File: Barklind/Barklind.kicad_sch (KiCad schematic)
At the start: 7 parts, among them J1 Molex 47053-1000, J2 Molex 47053-1000, J3 Molex 47053-1000, J4 RJ45_Abracon_ARJP11A-MASA-B-A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, J5 Conn_01x19, J6 Conn_01x19, U4 ESP32-DevKitC

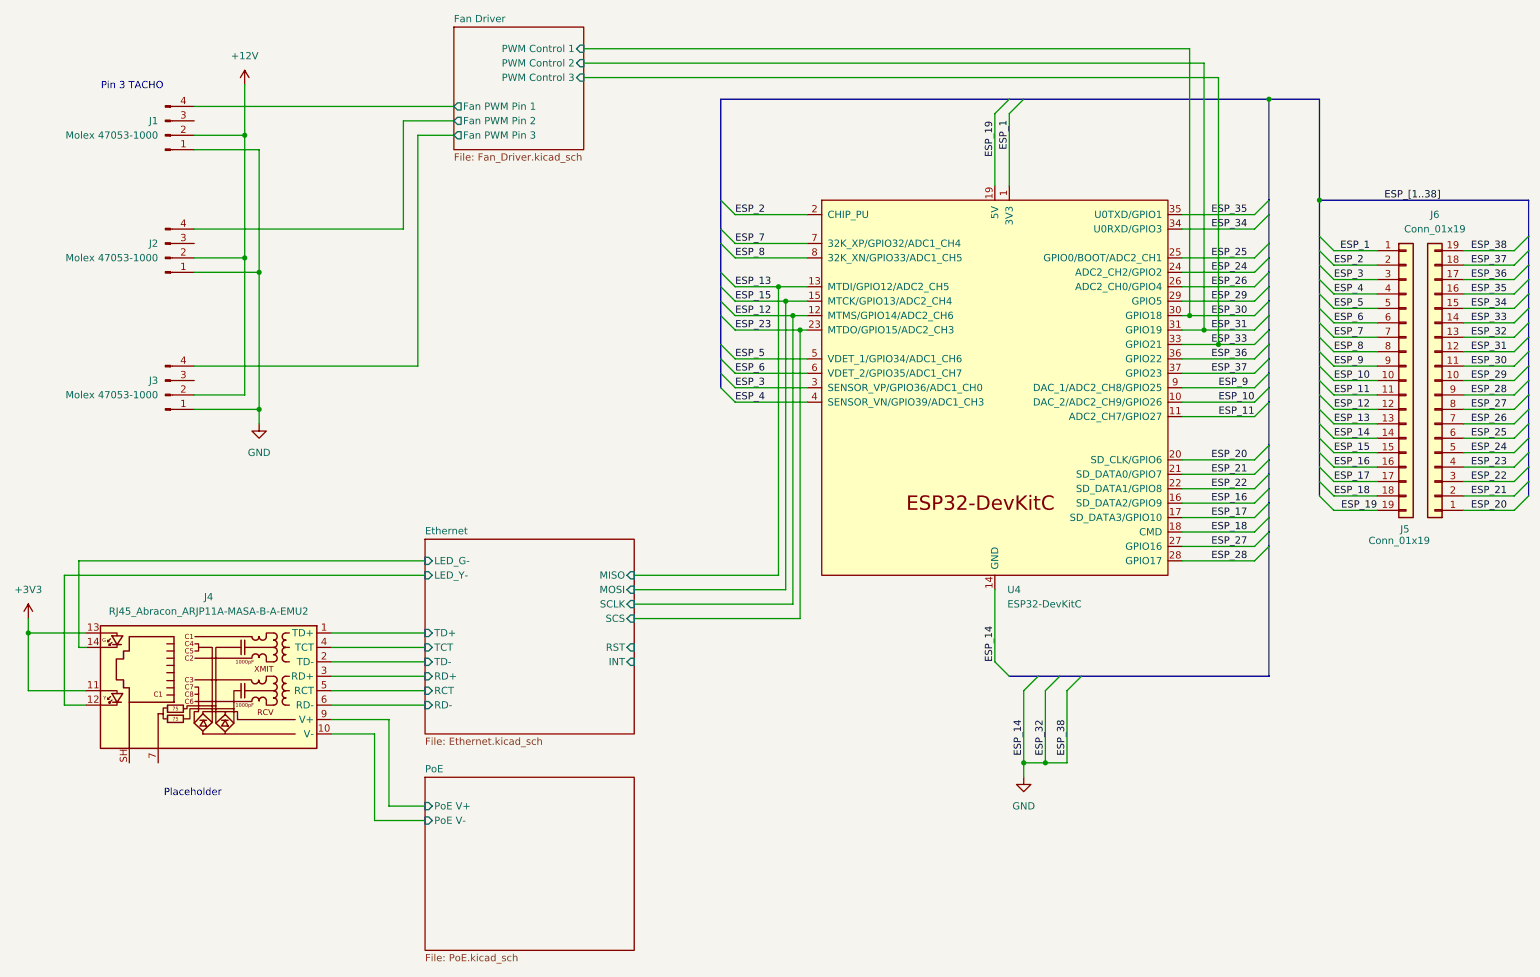
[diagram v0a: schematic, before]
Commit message: Added basic board (with no layout specified) Added additional comments to schematic
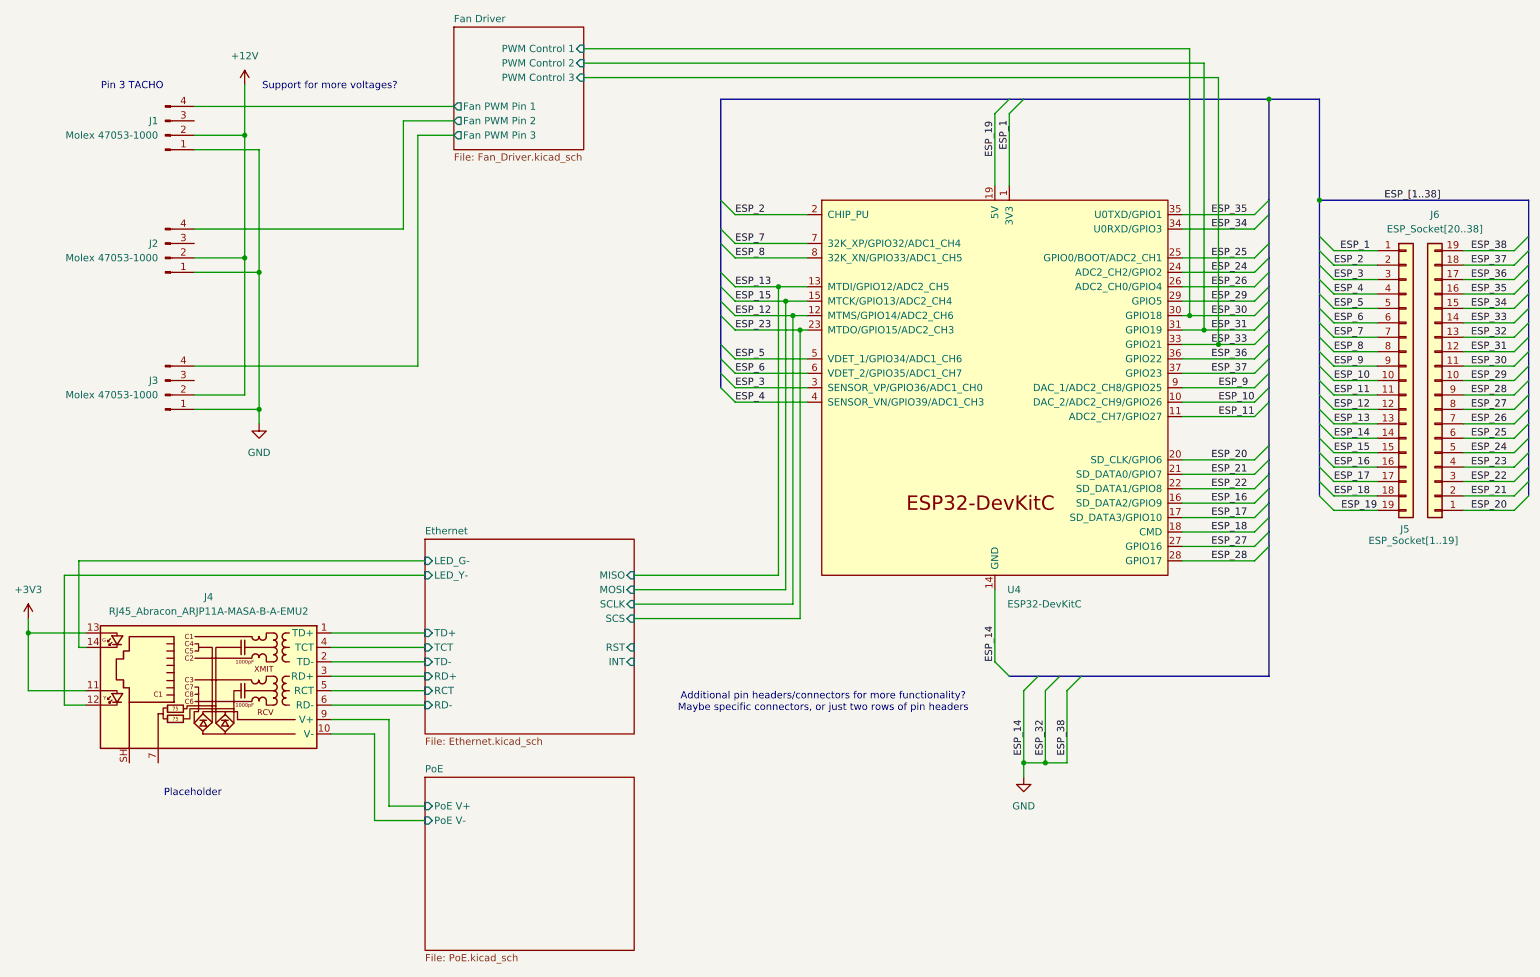
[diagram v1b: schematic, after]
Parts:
- J1, J2, J3: footprint (none) -> Connector:FanPinHeader_1x04_P2.54mm_Vertical
- J5: value Conn_01x19 -> ESP_Socket[1..19]; footprint (none) -> Connector_PinSocket_2.54mm:PinSocket_1x19_P2.54mm_Vertical
- J6: value Conn_01x19 -> ESP_Socket[20..38]; footprint (none) -> Connector_PinSocket_2.54mm:PinSocket_1x19_P2.54mm_Vertical
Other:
- note added: "Additional pin headers/connectors for more functionality? Maybe specific connectors, or just two rows of pin headers"
- note added: "Support for more voltages?"
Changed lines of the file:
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@@
+		)
+	)
+	(text "Support for more voltages?"
+		(exclude_from_sim no)
+		(at 68.326 38.354 0)
+		(effects
+			(font
+				(size 1.27 1.27)
+			)
 		)
 	)
@@
 		(exclude_from_sim no)
 		(at 44.196 162.814 0)
+		(effects
+			(font
+				(size 1.27 1.27)
+			)
+		)
+	)
+	(text "Additional pin headers/connectors for more functionality?\nMaybe specific connectors, or just two rows of pin headers\n"
+		(exclude_from_sim no)
+		(at 155.194 146.812 0)
 		(effects
 			(font
@@
 			)
 		)
-		(property "Footprint" ""
+		(property "Footprint" "Connector:FanPinHeader_1x04_P2.54mm_Vertical"
 			(at 39.37 92.71 0)
 			(effects
@@
 			)
 		)
-		(property "Footprint" ""
+		(property "Footprint" "Connector:FanPinHeader_1x04_P2.54mm_Vertical"
 			(at 39.37 46.99 0)
 			(effects
@@
 			)
 		)
-		(property "Value" "Conn_01x19"
+		(property "Value" "ESP_Socket[1..19]"
 			(at 251.206 118.364 0)
 			(effects
@@
 			)
 		)
-		(property "Footprint" ""
+		(property "Footprint" "Connector_PinSocket_2.54mm:PinSocket_1x19_P2.54mm_Vertical"
 			(at 257.81 90.17 0)
 			(effects
@@
 			)
 		)
-		(property "Footprint" ""
+		(property "Footprint" "Connector:FanPinHeader_1x04_P2.54mm_Vertical"
 			(at 39.37 68.58 0)
 			(effects
@@
 		(on_board yes)
 		(dnp no)
-		(fields_autoplaced yes)
 		(property "Reference" "J6"
 			(at 262.89 60.96 0)
@@
 			)
 		)
-		(property "Value" "Conn_01x19"
+		(property "Value" "ESP_Socket[20..38]"
 			(at 262.89 63.5 0)
 			(effects
@@
 			)
 		)
-		(property "Footprint" ""
+		(property "Footprint" "Connector_PinSocket_2.54mm:PinSocket_1x19_P2.54mm_Vertical"
 			(at 262.89 90.17 0)
 			(effects

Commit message: Restructured project, Changed kibot configurations into different files Changed github actions for the different jobs
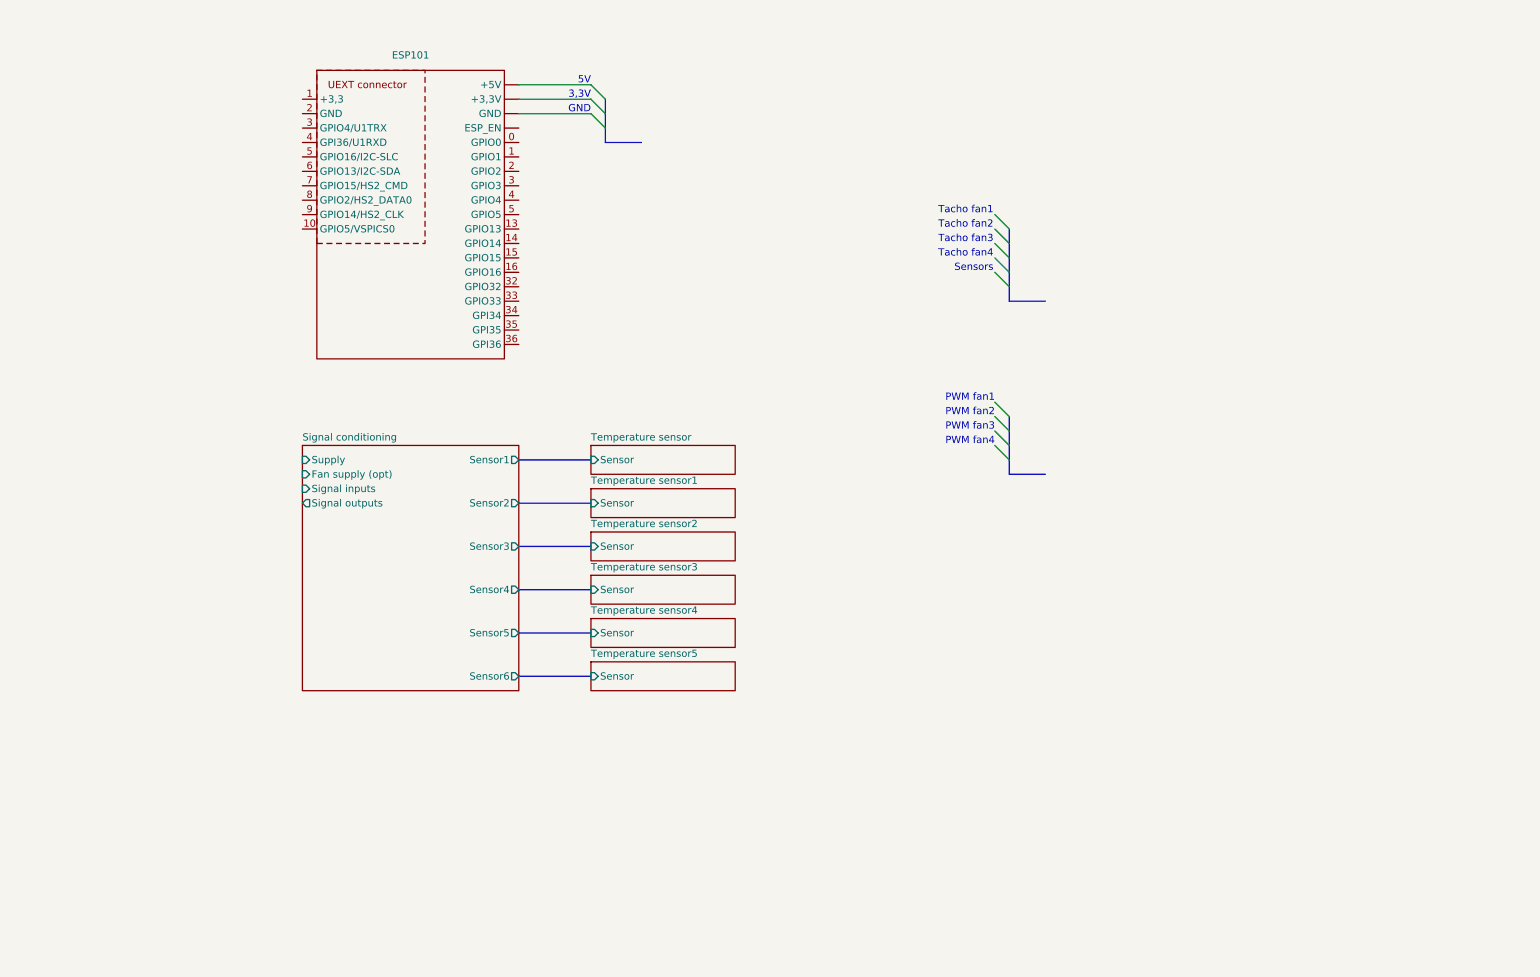
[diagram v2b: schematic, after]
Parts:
- removed J1, J2, J3: Molex 47053-1000, Connector:FanPinHeader_1x04_P2.54mm_Vertical, symbol Connector:Conn_01x04_Pin
- removed J4: RJ45_Abracon_ARJP11A-MASA-B-A-EMU2, Connector_RJ:RJ45_Abracon_ARJP11A-MA_Horizontal, symbol Connector:RJ45_Abracon_ARJP11A-MASA-B-A-EMU2
- removed J5: ESP_Socket[1..19], Connector_PinSocket_2.54mm:PinSocket_1x19_P2.54mm_Vertical, symbol Connector_Generic:Conn_01x19
- removed J6: ESP_Socket[20..38], Connector_PinSocket_2.54mm:PinSocket_1x19_P2.54mm_Vertical, symbol Connector_Generic:Conn_01x19
- removed U4: ESP32-DevKitC, PCM_Espressif:ESP32-DevKitC, symbol ESP32-Symbols:ESP32-DevKitC
- added ESP101: ~, symbol Own_ESP32:ESP32-POE-ISO
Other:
- removed sheet Ethernet
- removed sheet Fan Driver
- removed sheet PoE
- added sheet Signal conditioning (Signal conditioning.kicad_sch)
- added sheet Temperature sensor (Temperature sensor.kicad_sch)
- added sheet Temperature sensor1 (Temperature sensor.kicad_sch)
- added sheet Temperature sensor2 (Temperature sensor.kicad_sch)
- added sheet Temperature sensor3 (Temperature sensor.kicad_sch)
- added sheet Temperature sensor4 (Temperature sensor.kicad_sch)
- added sheet Temperature sensor5 (Temperature sensor.kicad_sch)
- note added: "3,3V"
- note added: "5V"
- note added: "GND"
- note added: "PWM fan1"
- note added: "PWM fan2"
- note added: "PWM fan3"
- note added: "PWM fan4"
- note added: "Sensors"
- note added: "Tacho fan1"
- note added: "Tacho fan2"
- note added: "Tacho fan3"
- note added: "Tacho fan4"
- note removed: "Additional pin headers/connectors for more functionality? Maybe specific connectors, or just two rows of pin headers"
- note removed: "Pin 3 TACHO"
- note removed: "Placeholder"
- note removed: "Support for more voltages?"

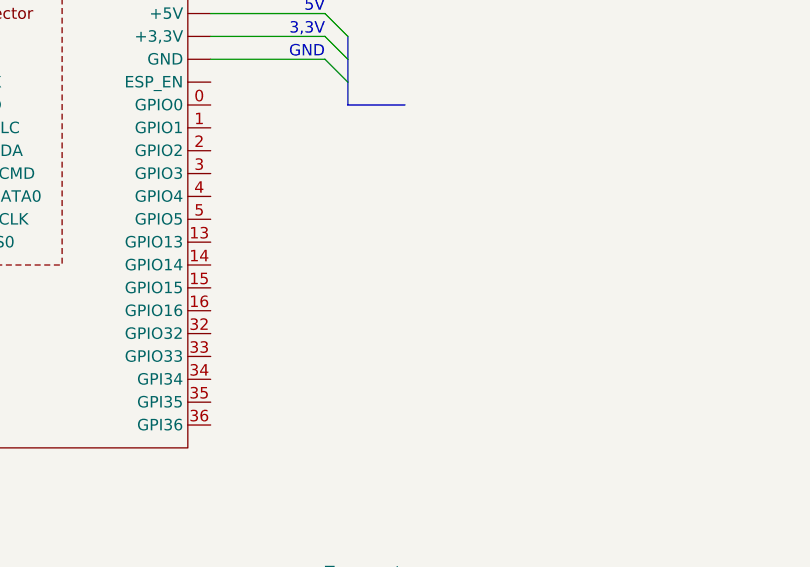
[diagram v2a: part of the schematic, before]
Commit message: Added text to schematic to troubleshoot workflow
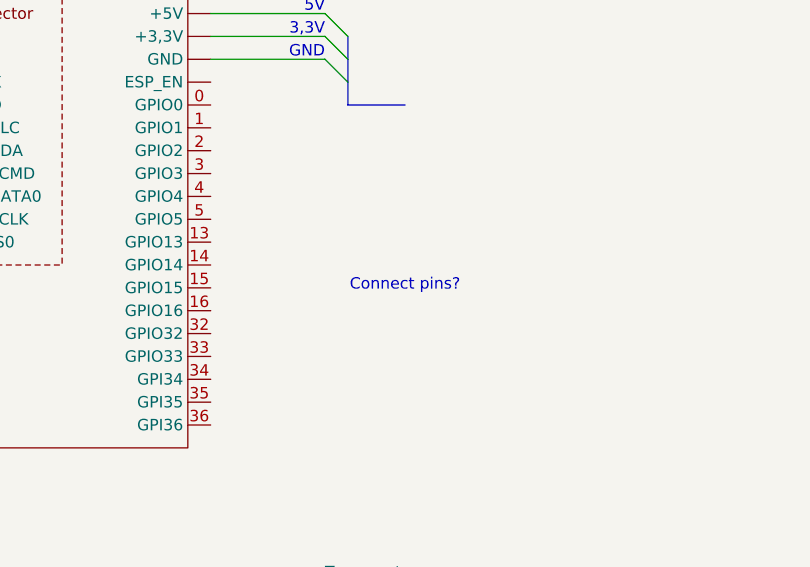
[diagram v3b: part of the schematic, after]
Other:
- note added: "Connect pins?"
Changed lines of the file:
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@@
+		)
+	)
+	(text "Connect pins?"
+		(exclude_from_sim no)
+		(at 123.19 68.326 0)
+		(effects
+			(font
+				(size 1.27 1.27)
+			)
 		)
 	)
@@
 		)
 		(instances
-			(project "POE ESP32 with 4 fans"
+			(project "Barklind"
 				(path "/693bf934-563d-494c-8702-b1400b481044"
 					(page "6")
@@
 		)
 		(instances
-			(project "POE ESP32 with 4 fans"
+			(project "Barklind"
 				(path "/693bf934-563d-494c-8702-b1400b481044"
 					(page "4")
@@
 		)
 		(instances
-			(project "POE ESP32 with 4 fans"
+			(project "Barklind"
 				(path "/693bf934-563d-494c-8702-b1400b481044"
 					(page "5")
@@
 		)
 		(instances
-			(project "POE ESP32 with 4 fans"
+			(project "Barklind"
 				(path "/693bf934-563d-494c-8702-b1400b481044"
 					(page "7")
@@
 		)
 		(instances
-			(project "POE ESP32 with 4 fans"
+			(project "Barklind"
 				(path "/693bf934-563d-494c-8702-b1400b481044"
 					(page "3")
@@
 		)
 		(instances
-			(project "POE ESP32 with 4 fans"
+			(project "Barklind"
 				(path "/693bf934-563d-494c-8702-b1400b481044"
 					(page "2")
@@
 		)
 		(instances
-			(project "POE ESP32 with 4 fans"
+			(project "Barklind"
 				(path "/693bf934-563d-494c-8702-b1400b481044"
 					(page "8")
